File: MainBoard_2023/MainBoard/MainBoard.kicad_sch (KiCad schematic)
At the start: 54 parts, among them IC1 IP2721D, J1 UJC-HP-3-SMT-TR, J2 Conn_01x03, J3 Barrel_Jack, J4 Conn_01x02, J5 Micro_SD_Card_Det_Hirose_DM3AT, J6 Micro_SD_Card_Det_Hirose_DM3AT, Q1 AO3400A, SW1 RS_PRO_Slide_Switch, U1 SEN0516, U2 Adafruit_BNO055_STEMMA_QT, U3 Seeed_Studio_XIAO_nRF52840_Se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, U4 Pi Pico 0, U5 Pi Pico 0

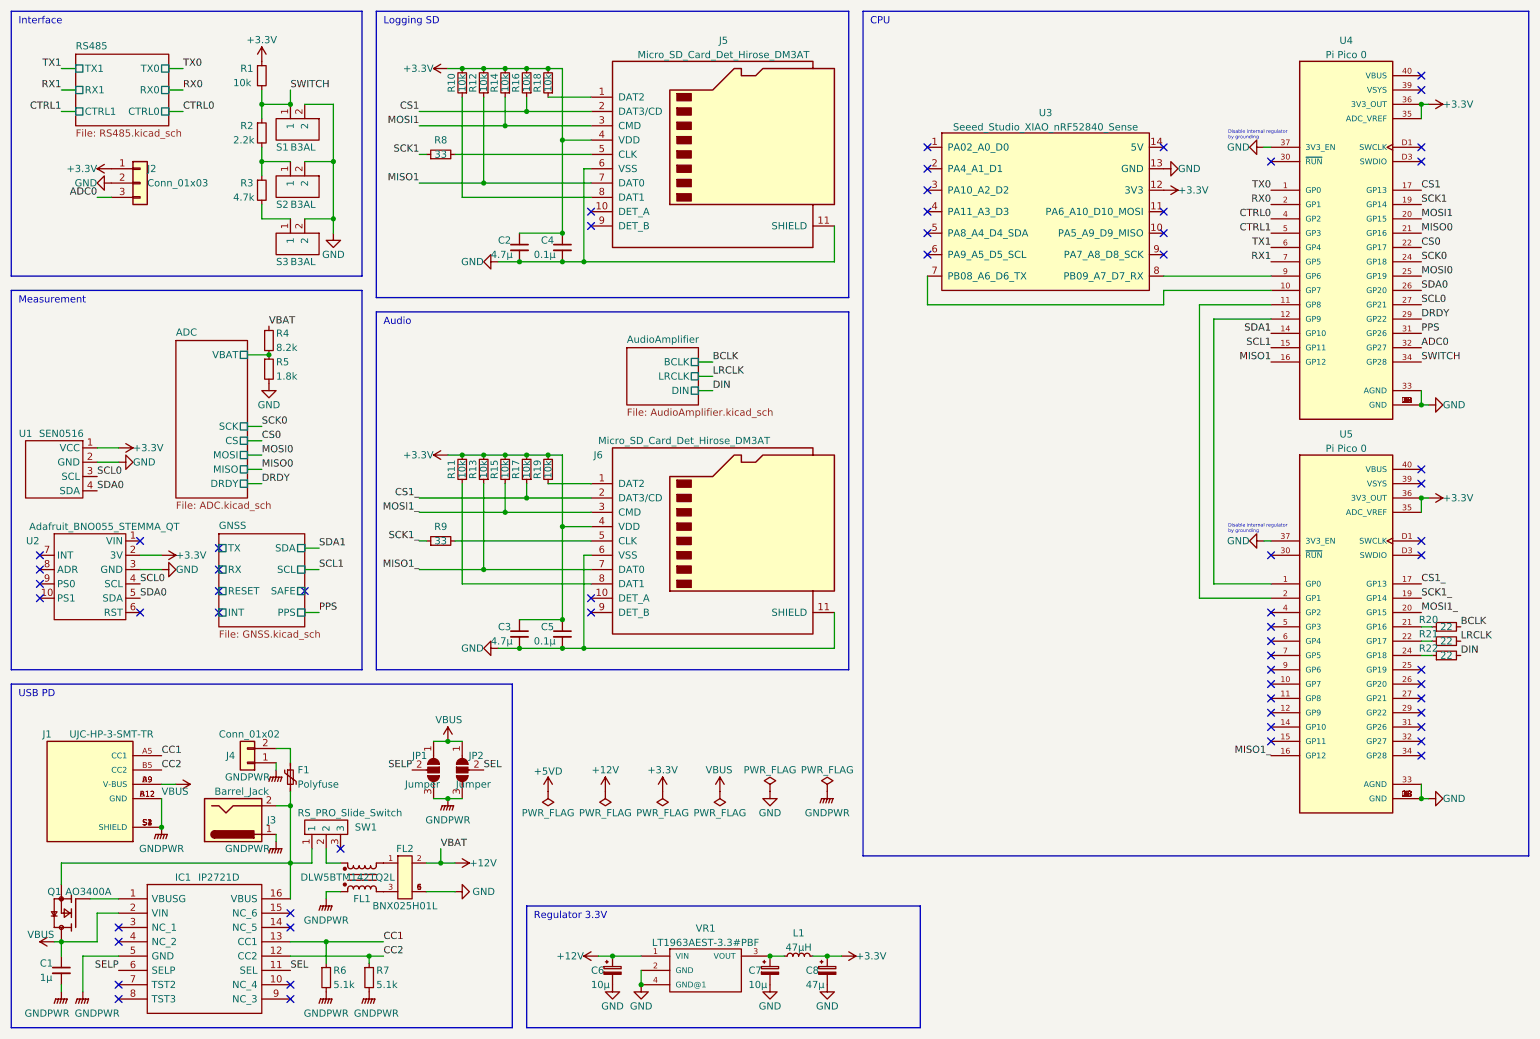
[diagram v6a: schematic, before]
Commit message: フットプリントをすべて割り当て
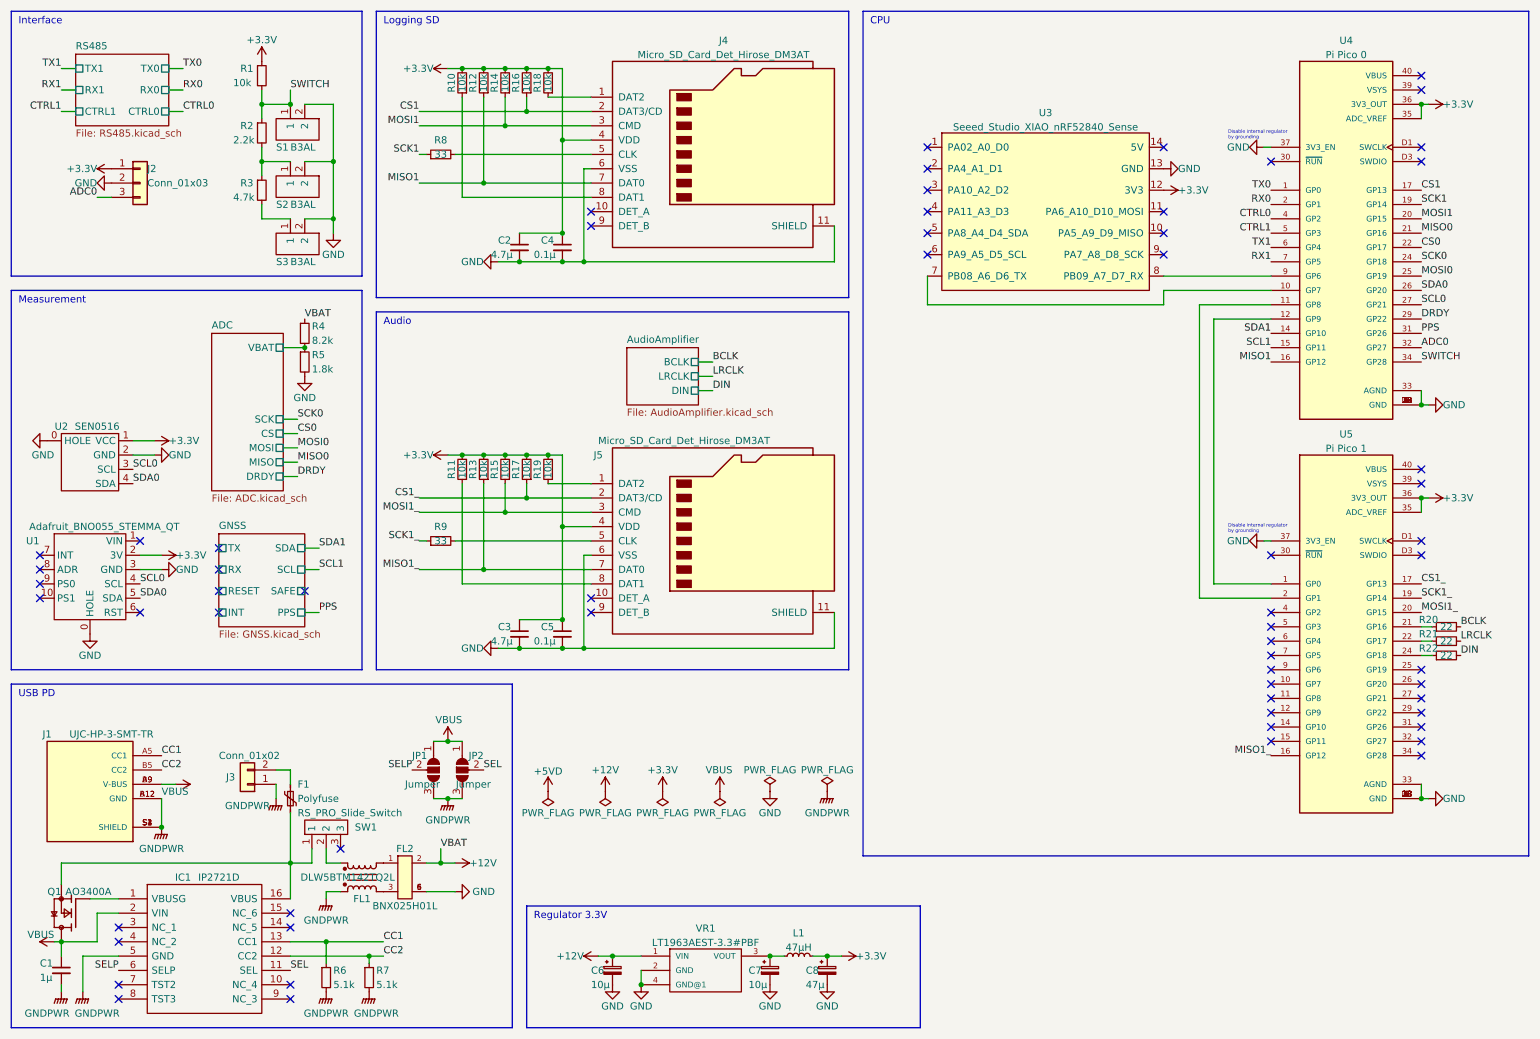
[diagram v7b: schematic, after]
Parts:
- removed J3: Barrel_Jack, symbol Connector:Barrel_Jack
- C1, C2, C3, C4, C5: footprint (none) -> Capacitor_SMD:C_0603_1608Metric_Pad1.08x0.95mm_HandSolder
- C6, C7: footprint (none) -> Capacitor_THT:CP_Radial_D6.3mm_P2.50mm
- C8: footprint (none) -> Capacitor_THT:CP_Radial_D10.0mm_P5.00mm
- F1: footprint (none) -> MF-R300:MF-R300
- FL1: footprint FIL_DLW5BTM142TQ2L -> DLW5BTM142TQ2:DLW5BTM142TQ2
- FL2: footprint FIL_BNX025H01L -> BNX025H01:BNX025H01
- IC1: footprint SOP65P640X120-16N -> IP2721:IP2721
- J1: footprint CUI_UJC-HP-3-SMT-TR -> USB_TypeC_6PIN:USB_TypeC_6PIN
- J2: footprint (none) -> B03B-PASK-1:B03B-PASK-1
- J3: renamed from J4; footprint (none) -> Connector_AMASS:AMASS_XT30PW-M_1x02_P2.50mm_Horizontal
- J4: renamed from J5; footprint (none) -> Connector_Card:microSD_HC_Hirose_DM3AT-SF-PEJM5
- J5: renamed from J6; footprint (none) -> Connector_Card:microSD_HC_Hirose_DM3AT-SF-PEJM5
- JP1, JP2: footprint (none) -> Jumper:SolderJumper-3_P2.0mm_Open_TrianglePad1.0x1.5mm_NumberLabels
- L1: footprint (none) -> NR10050T470M:NR10050T470M
- Q1: footprint SOT95P280X125-3N -> AO3400A:AO3400A
- R1, R10, R11, R12, R13, R14, R15, R16, R17, R18, R19, R2, R20, R21, R22, R3, R4, R5, R6, R7, R8, R9: footprint (none) -> Resistor_SMD:R_0603_1608Metric_Pad0.98x0.95mm_HandSolder
- S1, S2, S3: footprint B3AL1002PMS -> B3AL-1002P-MS:B3AL-1002P-MS
- SW1: footprint (none) -> RS_PRO_PCB_Slide_Switch_SPDT_Latching_3A_120V_ac_Top:RS_PRO_PCB_Slide_Switch_SPDT_Latching_3A_120V_ac_Top
- U1: renamed from U2; footprint (none) -> Adafruit_BNO055_STEMMA_QT:Adafruit_BNO055_STEMMA_QT
- U2: renamed from U1; footprint (none) -> Fermion_Pressure_Sensor_ICP_10111:Fermion_Pressure_Sensor_ICP_10111
- U3: footprint (none) -> Seeed_Studio_XIAO_nRF52840_Sense:Seeed_Studio_XIAO_nRF52840_Sense
- U4: footprint MODULE_SC0915 -> Raspberry_Pi_Pico:Raspberry_Pi_Pico
- U5: value Pi Pico 0 -> Pi Pico 1; footprint MODULE_SC0915 -> Raspberry_Pi_Pico:Raspberry_Pi_Pico
- VR1: footprint SOT223 -> LT1963AEST-3.3_PBF:LT1963AEST-3.3_PBF
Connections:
- net GND: now also U1.0 (HOLE), U2.0 (HOLE)
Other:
- moved on the sheet: F1, J3, R4, R5

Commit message: 部品配置中　モジュラーコネクタを廃止
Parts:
- F1: footprint MF-R300:MF-R300 -> ASMDC300F_24-2:ASMDC300F_24-2
